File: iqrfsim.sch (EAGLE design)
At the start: 8 parts

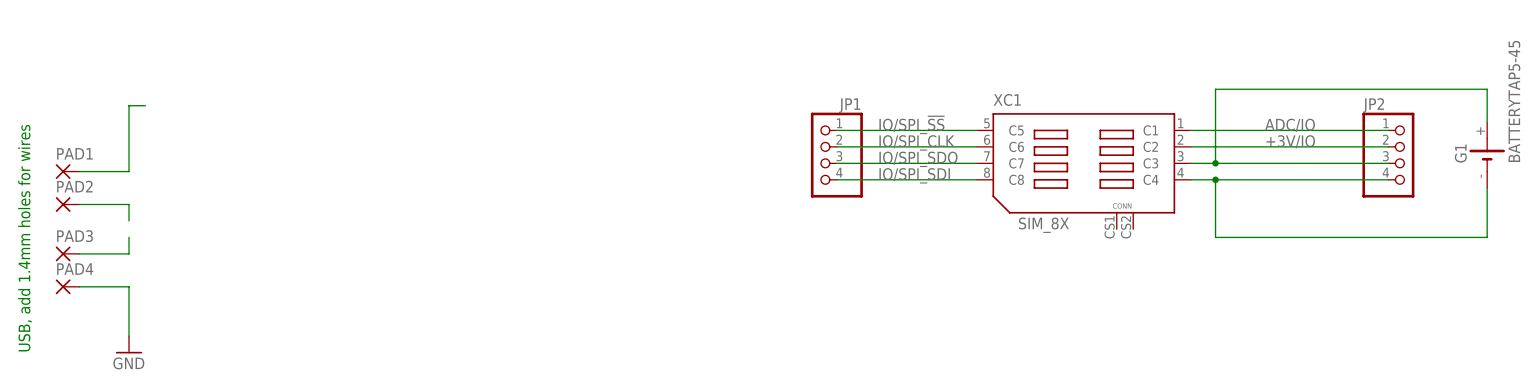
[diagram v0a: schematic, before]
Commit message: Fix iqrfsim sinal names, add board layout
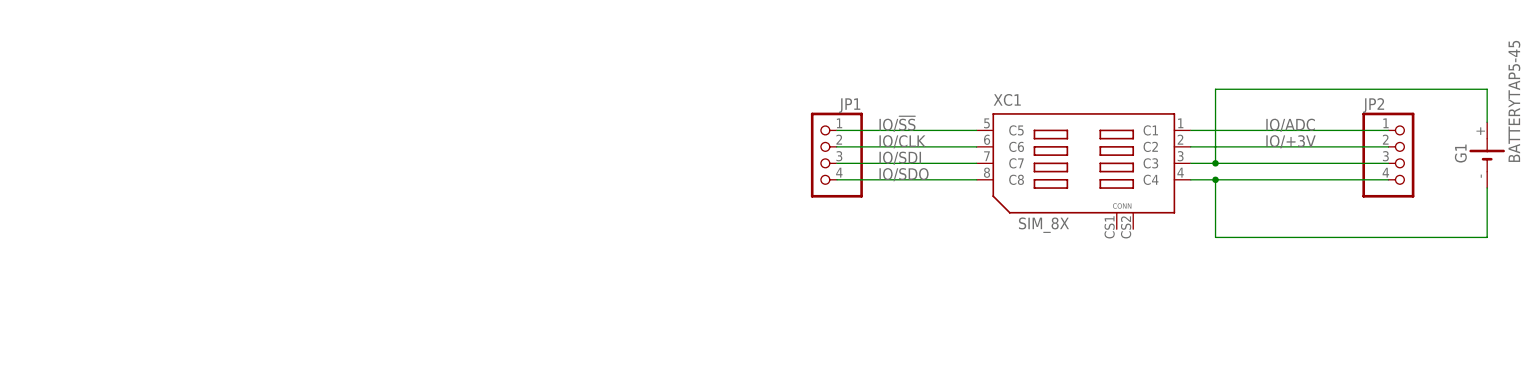
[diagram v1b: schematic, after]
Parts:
- removed PAD1, PAD2, PAD3, PAD4: (no value), wirepad:1,6/0,9
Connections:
- net +3V/IO renamed IO/+3V
- net ADC/IO renamed IO/ADC
- net IO/SPI_!SS renamed IO/!SS
- net IO/SPI_CLK renamed IO/CLK
- net IO/SPI_SDI renamed IO/SDO
- net IO/SPI_SDO renamed IO/SDI
- net N$1 renamed VIN
- removed net N$2: PAD3.P
- removed net N$3: PAD2.P
- removed net N$4: G1.-, JP2.4, XC1.C4
- removed net N$5: PAD1.P
- net GND: now also G1.-, JP2.4, XC1.C4; no longer PAD4.P
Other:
- note removed: "USB, add 1.4mm holes for wires"
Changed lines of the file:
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@@
 <setting verticaltext="up"/>
 </settings>
-<grid distance="0.05" unitdist="inch" unit="inch" style="lines" multiple="1" display="no" altdistance="0.01" altunitdist="inch" altunit="inch"/>
+<grid distance="0.1" unitdist="inch" unit="inch" style="lines" multiple="1" display="no" altdistance="0.01" altunitdist="inch" altunit="inch"/>
 <layers>
 <layer number="1" name="Top" color="4" fill="1" visible="no" active="no"/>
@@
 </classes>
 <parts>
-<part name="GND1" library="usbpiclib" deviceset="GND" device=""/>
-<part name="PAD1" library="wirepad" deviceset="1,6/0,9" device=""/>
-<part name="PAD2" library="wirepad" deviceset="1,6/0,9" device=""/>
-<part name="PAD3" library="wirepad" deviceset="1,6/0,9" device=""/>
-<part name="PAD4" library="wirepad" deviceset="1,6/0,9" device=""/>
 <part name="XC1" library="usbpiclib" deviceset="SIM_8X" device=""/>
 <part name="JP2" library="pinhead" deviceset="PINHD-1X4" device=""/>
@@
 <sheet>
 <plain>
-<text x="-127" y="30.48" size="1.778" layer="91" rot="R90">USB, add 1.4mm holes for wires</text>
 </plain>
 <instances>
-<instance part="GND1" gate="1" x="-111.76" y="30.48"/>
-<instance part="PAD1" gate="1" x="-121.92" y="58.42"/>
-<instance part="PAD2" gate="1" x="-121.92" y="53.34"/>
-<instance part="PAD3" gate="1" x="-121.92" y="45.72"/>
-<instance part="PAD4" gate="1" x="-121.92" y="40.64"/>
 <instance part="XC1" gate="G$1" x="33.02" y="63.5"/>
 <instance part="JP2" gate="A" x="85.09" y="59.69"/>
@@
 </busses>
 <nets>
-<net name="GND" class="0">
-<segment>
-<pinref part="GND1" gate="1" pin="GND"/>
-<pinref part="PAD4" gate="1" pin="P"/>
-<wire x1="-119.38" y1="40.64" x2="-111.76" y2="40.64" width="0.1524" layer="91"/>
-<wire x1="-111.76" y1="40.64" x2="-111.76" y2="33.02" width="0.1524" layer="91"/>
-</segment>
-</net>
-<net name="N$2" class="0">
-<segment>
-<pinref part="PAD3" gate="1" pin="P"/>
-<wire x1="-119.38" y1="45.72" x2="-111.76" y2="45.72" width="0.1524" layer="91"/>
-<wire x1="-111.76" y1="45.72" x2="-111.76" y2="48.26" width="0.1524" layer="91"/>
-</segment>
-</net>
-<net name="N$3" class="0">
-<segment>
-<pinref part="PAD2" gate="1" pin="P"/>
-<wire x1="-119.38" y1="53.34" x2="-111.76" y2="53.34" width="0.1524" layer="91"/>
-<wire x1="-111.76" y1="53.34" x2="-111.76" y2="50.8" width="0.1524" layer="91"/>
-</segment>
-</net>
-<net name="N$5" class="0">
-<segment>
-<wire x1="-111.76" y1="68.58" x2="-109.22" y2="68.58" width="0.1524" layer="91"/>
-<wire x1="-111.76" y1="58.42" x2="-111.76" y2="68.58" width="0.1524" layer="91"/>
-<pinref part="PAD1" gate="1" pin="P"/>
-<wire x1="-119.38" y1="58.42" x2="-111.76" y2="58.42" width="0.1524" layer="91"/>
-</segment>
-</net>
-<net name="IO/SPI_SDI" class="0">
+<net name="IO/SDO" class="0">
 <segment>
 <label x="3.81" y="57.15" size="1.778" layer="95"/>
@@
 </segment>
 </net>
-<net name="IO/SPI_CLK" class="0">
+<net name="IO/CLK" class="0">
 <segment>
 <label x="3.81" y="62.23" size="1.778" layer="95"/>
@@
 </segment>
 </net>
-<net name="IO/SPI_SDO" class="0">
+<net name="IO/SDI" class="0">
 <segment>
 <label x="3.81" y="59.69" size="1.778" layer="95"/>
@@
 </segment>
 </net>
-<net name="IO/SPI_!SS" class="0">
+<net name="IO/!SS" class="0">
 <segment>
 <label x="3.81" y="64.77" size="1.778" layer="95"/>
@@
 </segment>
 </net>
-<net name="+3V/IO" class="0">
+<net name="IO/+3V" class="0">
 <segment>
 <pinref part="XC1" gate="G$1" pin="C2"/>
@@
 </segment>
 </net>
-<net name="ADC/IO" class="0">
+<net name="IO/ADC" class="0">
 <segment>
 <pinref part="XC1" gate="G$1" pin="C1"/>
@@
 </segment>
 </net>
-<net name="N$1" class="0">
+<net name="VIN" class="0">
 <segment>
 <wire x1="55.88" y1="71.12" x2="55.88" y2="59.69" width="0.1524" layer="91"/>
@@
 </segment>
 </net>
-<net name="N$4" class="0">
+<net name="GND" class="0">
 <segment>
 <pinref part="XC1" gate="G$1" pin="C4"/>

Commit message: Finish iqrfsim.brd for manufacture
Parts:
- removed G1: BATTERYTAP5-45, tagps:BATTERYTAP5-45
- added GND, VIN: (no value), wirepad:1,6/0,9
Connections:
- net GND: now also GND.P; no longer G1.-
- net VIN: now also VIN.P; no longer G1.+
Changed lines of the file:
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@@
 <part name="JP2" library="pinhead" deviceset="PINHD-1X4" device=""/>
 <part name="JP1" library="pinhead" deviceset="PINHD-1X4" device=""/>
-<part name="G1" library="tagps" deviceset="BATTERY" device="TAP5-45"/>
+<part name="VIN" library="wirepad" deviceset="1,6/0,9" device=""/>
+<part name="GND" library="wirepad" deviceset="1,6/0,9" device=""/>
 </parts>
 <sheets>
@@
 <instance part="JP2" gate="A" x="85.09" y="59.69"/>
 <instance part="JP1" gate="A" x="-5.08" y="59.69" rot="MR0"/>
-<instance part="G1" gate="G$1" x="97.79" y="60.96" rot="R90"/>
+<instance part="VIN" gate="1" x="55.88" y="71.12" rot="R270"/>
+<instance part="GND" gate="1" x="55.88" y="48.26" rot="R90"/>
 </instances>
 <busses>
@@
 <net name="VIN" class="0">
 <segment>
-<wire x1="55.88" y1="71.12" x2="55.88" y2="59.69" width="0.1524" layer="91"/>
+<wire x1="55.88" y1="68.58" x2="55.88" y2="59.69" width="0.1524" layer="91"/>
 <pinref part="XC1" gate="G$1" pin="C3"/>
 <wire x1="52.07" y1="59.69" x2="55.88" y2="59.69" width="0.1524" layer="91"/>
@@
 <pinref part="JP2" gate="A" pin="3"/>
 <junction x="55.88" y="59.69"/>
-<pinref part="G1" gate="G$1" pin="+"/>
-<wire x1="55.88" y1="71.12" x2="97.79" y2="71.12" width="0.1524" layer="91"/>
-<wire x1="97.79" y1="71.12" x2="97.79" y2="66.04" width="0.1524" layer="91"/>
+<pinref part="VIN" gate="1" pin="P"/>
 </segment>
 </net>
@@
 <pinref part="XC1" gate="G$1" pin="C4"/>
 <wire x1="52.07" y1="57.15" x2="55.88" y2="57.15" width="0.1524" layer="91"/>
-<wire x1="55.88" y1="57.15" x2="55.88" y2="48.26" width="0.1524" layer="91"/>
+<wire x1="55.88" y1="57.15" x2="55.88" y2="50.8" width="0.1524" layer="91"/>
 <pinref part="JP2" gate="A" pin="4"/>
 <wire x1="55.88" y1="57.15" x2="82.55" y2="57.15" width="0.1524" layer="91"/>
 <junction x="55.88" y="57.15"/>
-<pinref part="G1" gate="G$1" pin="-"/>
-<wire x1="55.88" y1="48.26" x2="97.79" y2="48.26" width="0.1524" layer="91"/>
-<wire x1="97.79" y1="48.26" x2="97.79" y2="55.88" width="0.1524" layer="91"/>
+<pinref part="GND" gate="1" pin="P"/>
 </segment>
 </net>
